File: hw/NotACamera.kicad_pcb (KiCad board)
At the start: 2 copper layers, 63.4 x 52 mm, 12 parts, among them P1 SAO, U1 7555

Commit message: Final changes to gerbers
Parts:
- P1: footprint Pin_Headers:Pin_Header_Straight_2x02 -> NAC:Pin_Header_Straight_2x02_SAO

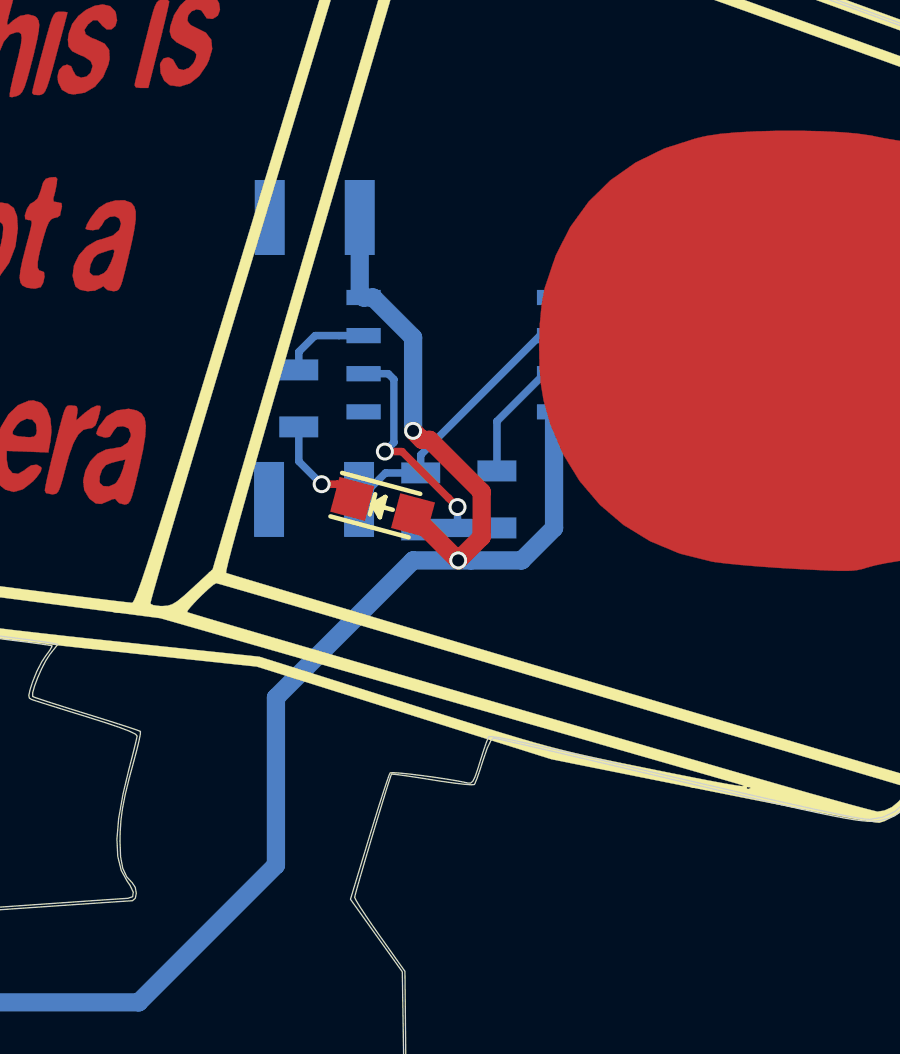
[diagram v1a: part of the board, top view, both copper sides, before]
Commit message: Finished new layout, moving old gerbers
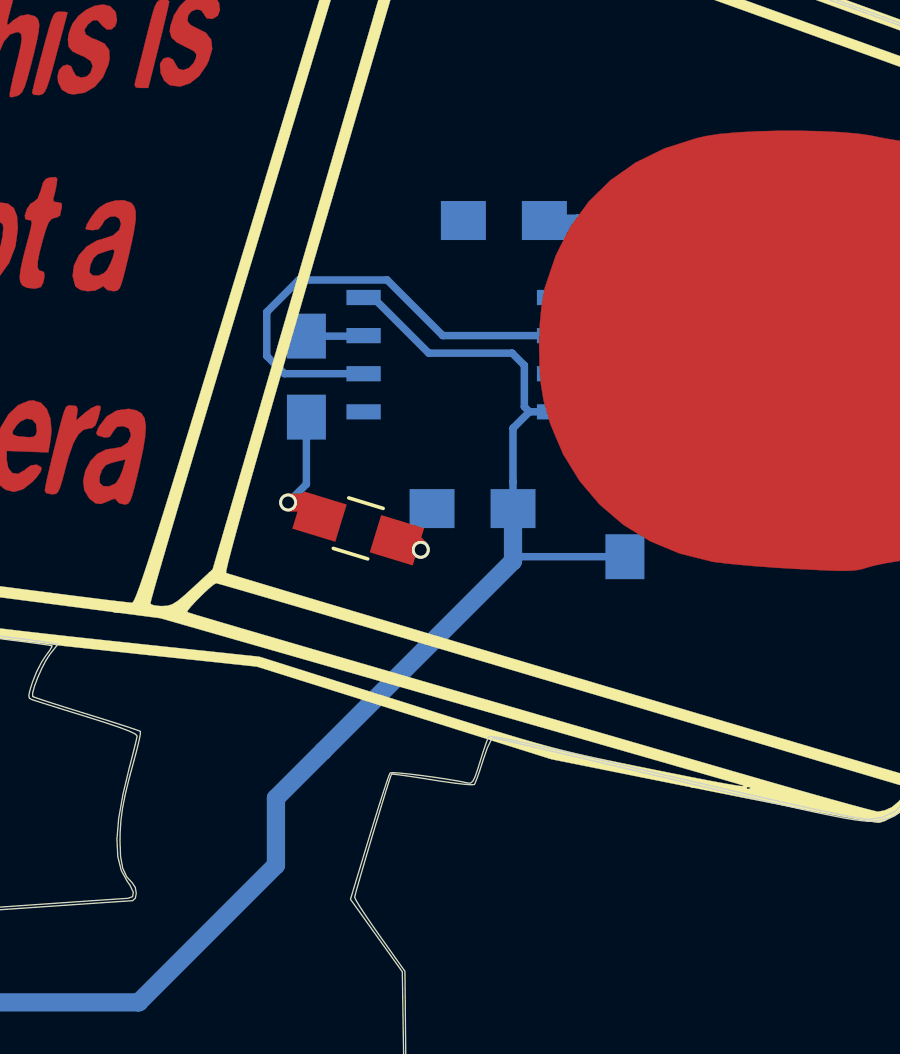
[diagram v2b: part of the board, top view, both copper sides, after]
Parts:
- C1, C2: footprint Capacitors_SMD:C_1210 -> Resistors_SMD:R_0805_HandSoldering
- D1: footprint LEDs:LED_0805 -> Resistors_SMD:R_0805_HandSoldering
- R1: value 1K8 -> 100; footprint Resistors_SMD:R_0805 -> Resistors_SMD:R_0805_HandSoldering
- R2: value 220K -> 100; footprint Resistors_SMD:R_0805 -> Resistors_SMD:R_0805_HandSoldering
- R3: value 1K8 -> 68K; footprint Resistors_SMD:R_0805 -> Resistors_SMD:R_0805_HandSoldering
- moved C1 11.2 mm to (126.0, 98.4)
- moved C2 11.0 mm to (124.9, 108.0)
- moved R3 8.45 mm to (130.0, 102.8)
- moved R2 4.30 mm to (130.0, 108.3), turned to 90 degrees
- moved D1 1.08 mm to (121.1, 108.7), turned to 163 degrees
- moved R1 0.77 mm to (119.4, 103.6)
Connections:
- D1 pad 1: Net-(D1-Pad1) -> /GND
- D1 pad 2: /VCC -> Net-(D1-Pad2)
- P1 pad 2: Net-(P1-Pad2) -> (no net)
- P1 pad 4: Net-(P1-Pad4) -> (no net)
- R1 pad 2: Net-(D1-Pad1) -> Net-(D1-Pad2)
- R2 pad 1: Net-(R2-Pad1) -> /VCC
- U1 pad 2: Net-(R2-Pad2) -> Net-(C1-Pad1)
- U1 pad 5: Net-(U1-Pad5) -> (no net)
- U1 pad 7: Net-(R2-Pad1) -> Net-(R2-Pad2)
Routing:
- net Net-(C1-Pad1): track 9.11 -> 23.3 mm
- net /VCC: track 72.4 -> 66.3 mm, vias 2 -> 0
- net Net-(R2-Pad2): track 10.1 -> 5.44 mm, vias 2 -> 0
- net Net-(D1-Pad2): track 0.00 -> 4.34 mm, vias 0 -> 1
- net Net-(R2-Pad1): track 4.22 -> 0.00 mm
- net Net-(D1-Pad1): track 3.45 -> 0.00 mm, vias 1 -> 0
- net /GND: track 0.00 -> 1.30 mm, vias 0 -> 1
- net Net-(R1-Pad1): track 2.98 -> 1.91 mm

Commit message: Created v1 gerbers
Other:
- rule pad_to_mask_clearance: 0.2 -> 0
- board text added: "Learn how to design & assemble this board: https://contextualelectronics.com/NAC"
- board text removed: "Instructions: https://contextualelectronics.com/NAC"
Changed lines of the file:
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@@
   (general
     (links 15)
-    (no_connects 6)
-    (area 0 0 0 0)
+    (no_connects 0)
+    (area 74.6125 84.328 148.971001 145.542001)
     (thickness 1.6)
     (drawings 1)
@@
     (pcb_text_size 1.5 1.5)
     (mod_edge_width 0.15)
-    (mod_text_size 0.8 0.8)
-    (mod_text_width 0.12)
+    (mod_text_size 0.635 0.635)
+    (mod_text_width 0.1016)
     (pad_size 1.524 1.524)
     (pad_drill 0.762)
-    (pad_to_mask_clearance 0.2)
+    (pad_to_mask_clearance 0)
     (aux_axis_origin 0 0)
     (visible_elements 7FFEFFFF)
@@
       (drillshape 0)
       (scaleselection 1)
-      (outputdirectory GerberV0/))
+      (outputdirectory GerberV1/))
   )
   (net 0 "")
@@
     )
     (fp_text value LOGO (at 0.75 0) (layer F.SilkS) hide
-      (effects (font (size 0.8 0.8) (thickness 0.12)))
+      (effects (font (size 0.635 0.635) (thickness 0.1016)))
     )
     (fp_poly (pts (xy 30.188567 -18.01329) (xy 30.774837 -17.204254) (xy 31.025371 -16.841558) (xy 31.213234 -16.535168)
@@
     )
     (fp_text value 7555 (at 0 -1.27 90) (layer B.Fab)
-      (effects (font (size 0.8 0.8) (thickness 0.12)) (justify mirror))
+      (effects (font (size 0.635 0.635) (thickness 0.1016)) (justify mirror))
     )
     (fp_line (start -2.54 2.286) (end 2.54 2.286) (layer B.SilkS) (width 0.15))
@@
     )
     (fp_text value LOGO (at 0.75 0) (layer F.SilkS) hide
-      (effects (font (size 0.8 0.8) (thickness 0.12)))
+      (effects (font (size 0.635 0.635) (thickness 0.1016)))
     )
     (fp_poly (pts (xy 19.223046 -22.103477) (xy 20.53532 -21.628863) (xy 21.80324 -21.170077) (xy 23.017743 -20.730408)
@@
     )
     (fp_text value LOGO (at 0.75 0) (layer F.Cu) hide
-      (effects (font (size 0.8 0.8) (thickness 0.12)))
+      (effects (font (size 0.635 0.635) (thickness 0.1016)))
     )
     (fp_poly (pts (xy 22.221922 -16.338399) (xy 22.879081 -16.307019) (xy 23.448012 -16.259229) (xy 23.893201 -16.195058)
@@
     )
     (fp_text value LOGO (at 0.75 0) (layer F.SilkS) hide
-      (effects (font (size 0.8 0.8) (thickness 0.12)))
+      (effects (font (size 0.635 0.635) (thickness 0.1016)))
     )
     (fp_poly (pts (xy 4.021666 1.669915) (xy 7.535333 2.708427) (xy 8.276611 2.928528) (xy 8.967994 3.135752)
@@
     )
     (fp_text value SAO (at 0 -3.1) (layer F.Fab)
-      (effects (font (size 0.8 0.8) (thickness 0.12)))
+      (effects (font (size 0.635 0.635) (thickness 0.1016)))
     )
     (fp_line (start -1.75 -1.75) (end -1.75 4.3) (layer F.CrtYd) (width 0.05))
@@
     )
     (fp_text value 10U (at 0 -1.75 180) (layer B.Fab)
-      (effects (font (size 1 1) (thickness 0.15)) (justify mirror))
+      (effects (font (size 0.635 0.635) (thickness 0.1016)) (justify mirror))
     )
     (fp_text user %R (at 0 0 180) (layer B.Fab)
-      (effects (font (size 0.5 0.5) (thickness 0.075)) (justify mirror))
+      (effects (font (size 0.635 0.635) (thickness 0.1016)) (justify mirror))
     )
     (fp_line (start -1 -0.62) (end -1 0.62) (layer B.Fab) (width 0.1))
@@
     )
     (fp_text value 10U (at 0 -1.75 180) (layer B.Fab)
-      (effects (font (size 1 1) (thickness 0.15)) (justify mirror))
+      (effects (font (size 0.635 0.635) (thickness 0.1016)) (justify mirror))
     )
     (fp_text user %R (at 0 0 180) (layer B.Fab)
-      (effects (font (size 0.5 0.5) (thickness 0.075)) (justify mirror))
+      (effects (font (size 0.635 0.635) (thickness 0.1016)) (justify mirror))
     )
     (fp_line (start -1 -0.62) (end -1 0.62) (layer B.Fab) (width 0.1))
@@
     )
     (fp_text value 100 (at 0 -1.75 270) (layer B.Fab)
-      (effects (font (size 1 1) (thickness 0.15)) (justify mirror))
+      (effects (font (size 0.635 0.635) (thickness 0.1016)) (justify mirror))
     )
     (fp_text user %R (at 0 0 270) (layer B.Fab)
-      (effects (font (size 0.5 0.5) (thickness 0.075)) (justify mirror))
+      (effects (font (size 0.635 0.635) (thickness 0.1016)) (justify mirror))
     )
     (fp_line (start -1 -0.62) (end -1 0.62) (layer B.Fab) (width 0.1))
@@
     )
     (fp_text value 100 (at 0 -1.75 90) (layer B.Fab)
-      (effects (font (size 1 1) (thickness 0.15)) (justify mirror))
+      (effects (font (size 0.635 0.635) (thickness 0.1016)) (justify mirror))
     )
     (fp_text user %R (at 0 0 90) (layer B.Fab)
-      (effects (font (size 0.5 0.5) (thickness 0.075)) (justify mirror))
+      (effects (font (size 0.635 0.635) (thickness 0.1016)) (justify mirror))
     )
     (fp_line (start -1 -0.62) (end -1 0.62) (layer B.Fab) (width 0.1))
@@
     )
     (fp_text value 68K (at 0 -1.75 90) (layer B.Fab)
-      (effects (font (size 1 1) (thickness 0.15)) (justify mirror))
+      (effects (font (size 0.635 0.635) (thickness 0.1016)) (justify mirror))
     )
     (fp_text user %R (at 0 0 90) (layer B.Fab)
-      (effects (font (size 0.5 0.5) (thickness 0.075)) (justify mirror))
+      (effects (font (size 0.635 0.635) (thickness 0.1016)) (justify mirror))
     )
     (fp_line (start -1 -0.62) (end -1 0.62) (layer B.Fab) (width 0.1))
@@
     )
     (fp_text value "GREEN LED" (at 0 1.75 163) (layer F.Fab)
-      (effects (font (size 1 1) (thickness 0.15)))
+      (effects (font (size 0.635 0.635) (thickness 0.1016)))
     )
     (fp_text user %R (at 0 0 163) (layer F.Fab)
-      (effects (font (size 0.5 0.5) (thickness 0.075)))
+      (effects (font (size 0.635 0.635) (thickness 0.1016)))
     )
     (fp_line (start -1 0.62) (end -1 -0.62) (layer F.Fab) (width 0.1))
@@
     )
   )
-  (gr_text "Instructions:\nhttps://contextualelectronics.com/NAC" (at 125.73 93.726 345) (layer B.SilkS)
+  (gr_text "Learn how to design & assemble this board:\nhttps://contextualelectronics.com/NAC" (at 122.2756 94.1832) (layer B.SilkS)
     (effects (font (size 1.016 1.016) (thickness 0.2032)) (justify mirror))
   )

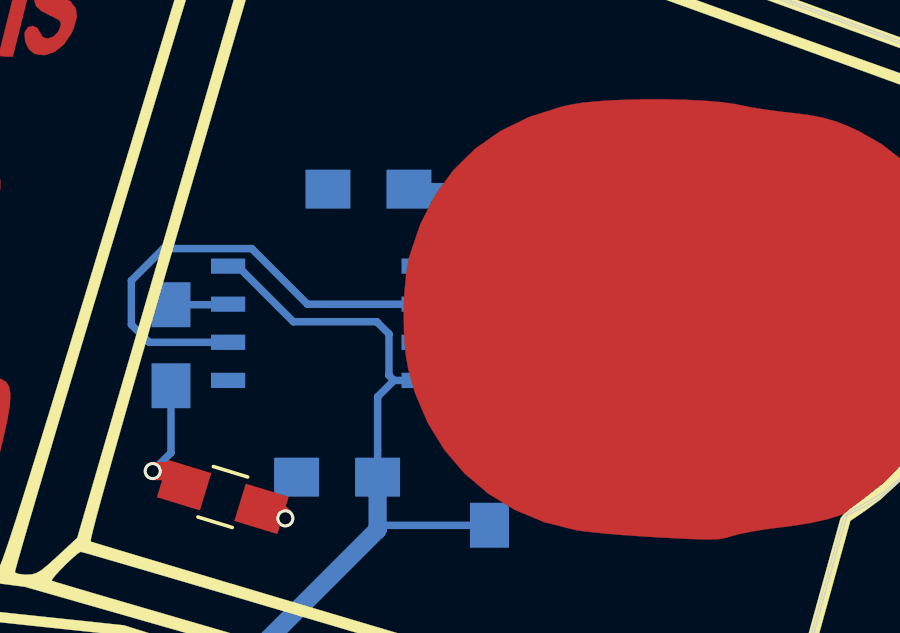
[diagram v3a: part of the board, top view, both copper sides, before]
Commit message: Tightened up some traces
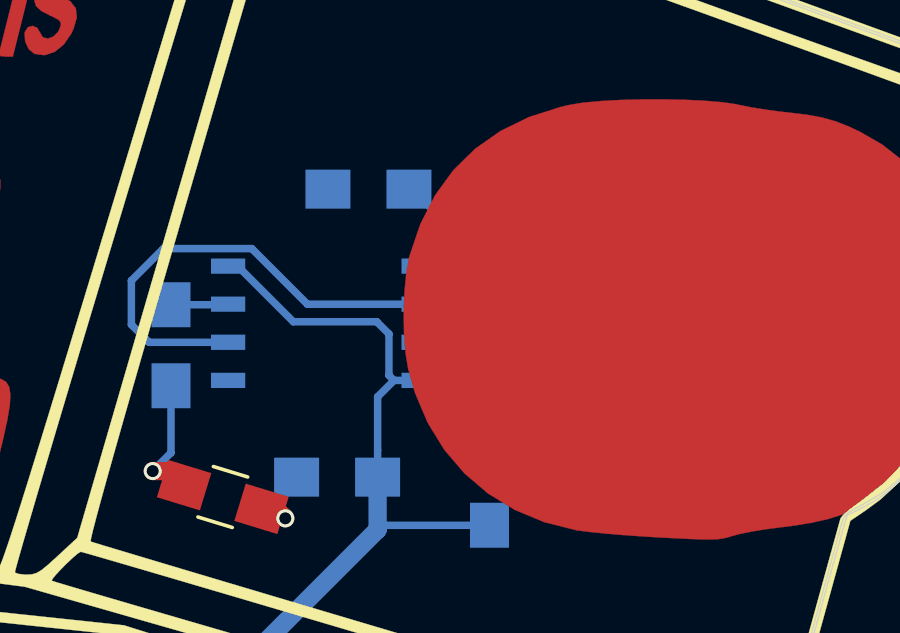
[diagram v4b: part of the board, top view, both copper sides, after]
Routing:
- net Net-(C1-Pad1): track 23.3 -> 22.7 mm
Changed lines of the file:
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@@
     (thickness 1.6)
     (drawings 1)
-    (tracks 49)
+    (tracks 48)
     (zones 0)
     (modules 12)
@@
   (page A4)
   (layers
-    (0 F.Cu signal)
+    (0 F.Cu signal hide)
     (31 B.Cu signal)
     (32 B.Adhes user)
@@
     (37 F.SilkS user)
     (38 B.Mask user)
-    (39 F.Mask user)
+    (39 F.Mask user hide)
     (40 Dwgs.User user)
     (41 Cmts.User user)
@@
   (segment (start 122.873502 109.055902) (end 123.19 109.3724) (width 0.6096) (layer F.Cu) (net 2))
   (via (at 123.19 109.3724) (size 0.6) (drill 0.4) (layers F.Cu B.Cu) (net 2))
+  (segment (start 127.3124 98.3996) (end 127.4124 98.3996) (width 0.25) (layer B.Cu) (net 3))
+  (segment (start 127.4124 98.3996) (end 130.048 101.0352) (width 0.25) (layer B.Cu) (net 3))
+  (segment (start 130.048 101.0352) (end 130.048 101.4692) (width 0.25) (layer B.Cu) (net 3))
   (segment (start 127.635 102.235) (end 129.2822 102.235) (width 0.25) (layer B.Cu) (net 3))
   (segment (start 129.2822 102.235) (end 130.048 101.4692) (width 0.25) (layer B.Cu) (net 3))
@@
   (segment (start 119.126 100.3808) (end 122.0724 100.3808) (width 0.25) (layer B.Cu) (net 3))
   (segment (start 122.0724 100.3808) (end 123.9266 102.235) (width 0.25) (layer B.Cu) (net 3))
-  (segment (start 128.4396 98.5012) (end 127.414 98.5012) (width 0.6096) (layer B.Cu) (net 3))
-  (segment (start 127.414 98.5012) (end 127.3124 98.3996) (width 0.6096) (layer B.Cu) (net 3))
-  (segment (start 130.048 101.4692) (end 130.048 100.1096) (width 0.6096) (layer B.Cu) (net 3))
-  (segment (start 130.048 100.1096) (end 128.4396 98.5012) (width 0.6096) (layer B.Cu) (net 3))
   (segment (start 119.38 102.2528) (end 121.2672 102.2528) (width 0.25) (layer B.Cu) (net 4))
   (segment (start 121.2672 102.2528) (end 121.285 102.235) (width 0.25) (layer B.Cu) (net 4))
-  (segment (start 127.635 103.505) (end 129.3838 103.505) (width 0.6096) (layer B.Cu) (net 5))
-  (segment (start 129.3838 103.505) (end 130.048 104.1692) (width 0.6096) (layer B.Cu) (net 5))
-  (segment (start 130.048 104.1692) (end 130.048 106.854) (width 0.6096) (layer B.Cu) (net 5))
-  (segment (start 130.048 106.854) (end 129.9972 106.9048) (width 0.6096) (layer B.Cu) (net 5))
+  (segment (start 130.048 104.1692) (end 130.048 106.854) (width 0.25) (layer B.Cu) (net 5))
+  (segment (start 130.048 106.854) (end 129.9972 106.9048) (width 0.25) (layer B.Cu) (net 5))
+  (segment (start 127.635 103.505) (end 129.3838 103.505) (width 0.25) (layer B.Cu) (net 5))
+  (segment (start 129.3838 103.505) (end 130.048 104.1692) (width 0.25) (layer B.Cu) (net 5))
   (segment (start 119.38 104.9528) (end 119.38 107.188) (width 0.25) (layer B.Cu) (net 6))
   (segment (start 119.38 107.188) (end 118.7704 107.7976) (width 0.25) (layer B.Cu) (net 6))
